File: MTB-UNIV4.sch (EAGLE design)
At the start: 116 parts, among them IC1 MEGA128-A, IC2 SN75176BP, IC3 MC7805CDTG, IC4 ULN2803A, IC5 ULN2803A, Q1 14.745 MHz, X1A MVE252-5-V, X1B MVE252-5-V, X2A MVE252-5-V, X2B MVE252-5-V, X3 1751316, X4 1751316, X5 1751316, X6 1751316

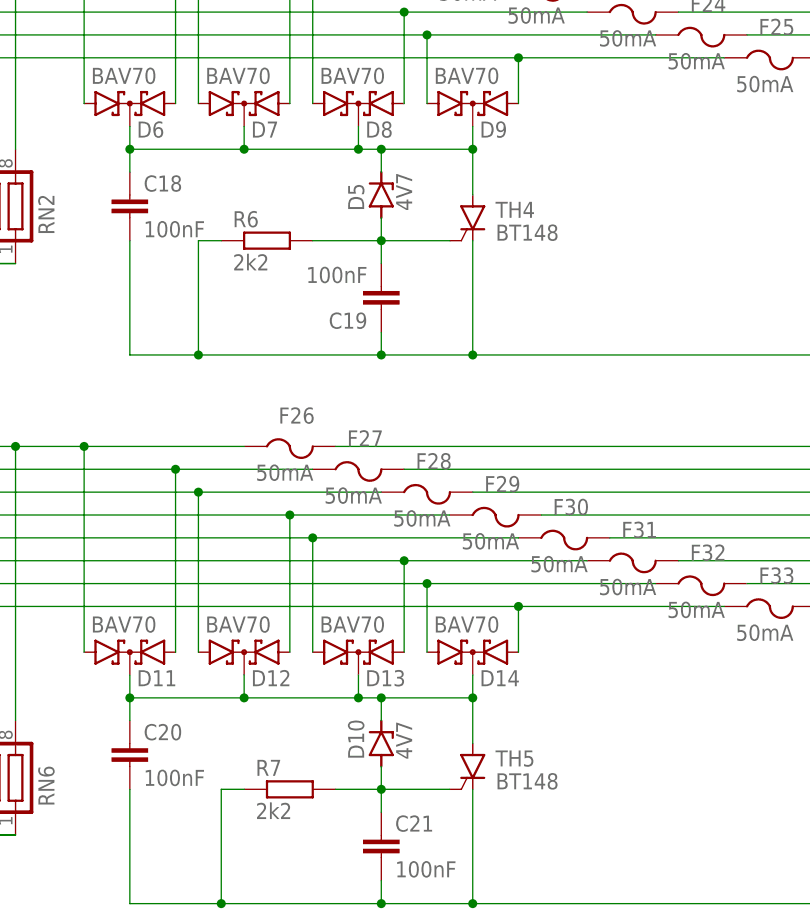
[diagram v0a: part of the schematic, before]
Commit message: Revert zener diodes on inputs to 5V1.
5V1 diodes open tyrristor at ~4V8.
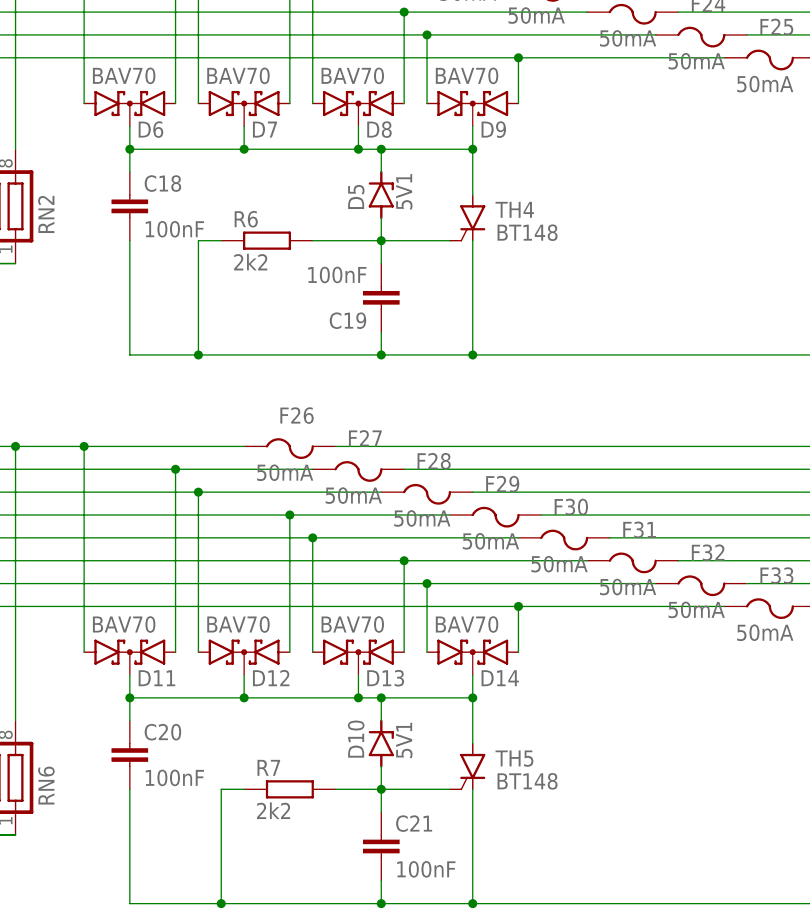
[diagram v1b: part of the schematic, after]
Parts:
- D10, D5: value 4V7 -> 5V1; LCSC_PART C384560 -> C294621
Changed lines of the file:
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@@
 <attribute name="LCSC_PART" value="C261946"/>
 </part>
-<part name="D5" library="diode" library_urn="urn:adsk.eagle:library:210" deviceset="ZENER-DIODE" device="SOT23" package3d_urn="urn:adsk.eagle:package:43389/2" value="4V7">
-<attribute name="LCSC_PART" value="C384560"/>
+<part name="D5" library="diode" library_urn="urn:adsk.eagle:library:210" deviceset="ZENER-DIODE" device="SOT23" package3d_urn="urn:adsk.eagle:package:43389/2" value="5V1">
+<attribute name="LCSC_PART" value="C294621"/>
 </part>
 <part name="R6" library="rcl" deviceset="R-EU_" device="R0805" value="2k2">
@@
 <attribute name="LCSC_PART" value="C261946"/>
 </part>
-<part name="D10" library="diode" library_urn="urn:adsk.eagle:library:210" deviceset="ZENER-DIODE" device="SOT23" package3d_urn="urn:adsk.eagle:package:43389/2" value="4V7">
-<attribute name="LCSC_PART" value="C384560"/>
+<part name="D10" library="diode" library_urn="urn:adsk.eagle:library:210" deviceset="ZENER-DIODE" device="SOT23" package3d_urn="urn:adsk.eagle:package:43389/2" value="5V1">
+<attribute name="LCSC_PART" value="C294621"/>
 </part>
 <part name="R7" library="rcl" deviceset="R-EU_" device="R0805" value="2k2">

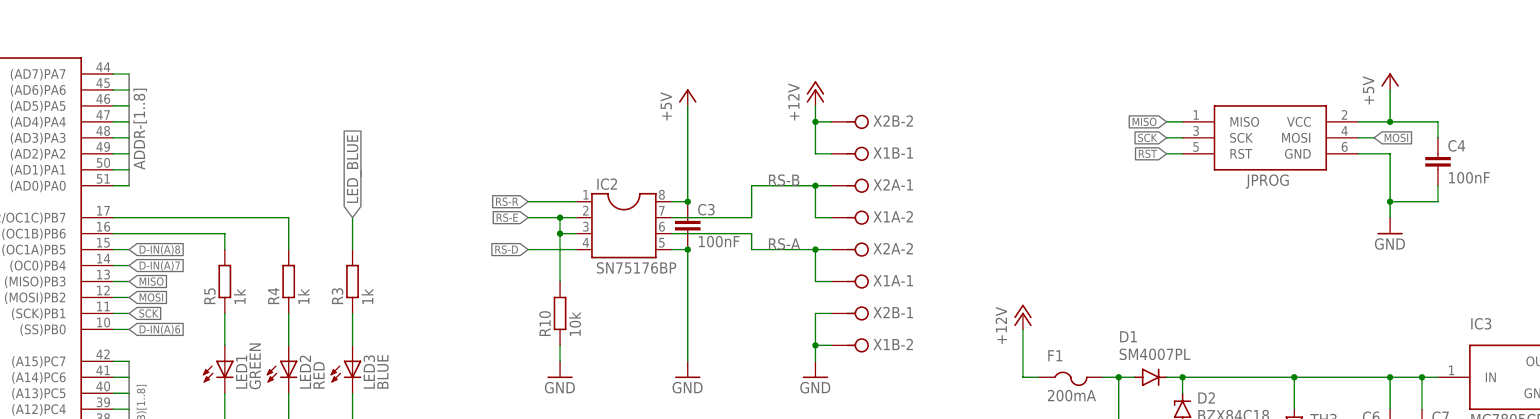
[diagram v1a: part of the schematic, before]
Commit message: Add right MCU pins to programming connector.
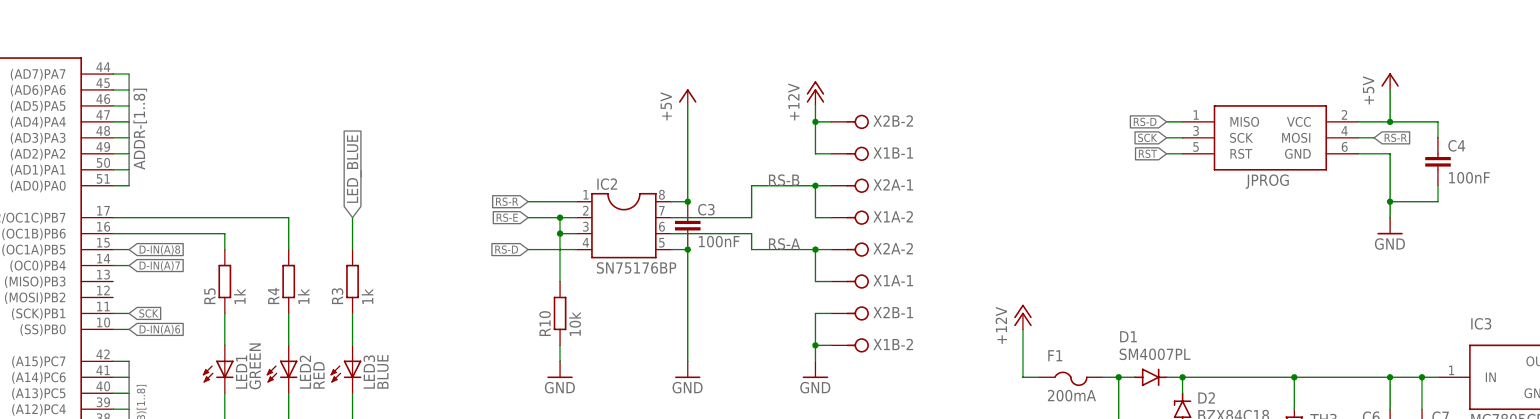
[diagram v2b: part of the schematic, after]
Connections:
- removed net MISO: IC1.(MISO)PB3, JPROG.MISO
- removed net MOSI: IC1.(MOSI)PB2, JPROG.MOSI
- net RS-D: now also JPROG.MISO
- net RS-R: now also JPROG.MOSI
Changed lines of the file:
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@@
-</segment>
-</net>
-<net name="MISO" class="0">
-<segment>
-<pinref part="IC1" gate="G$1" pin="(MISO)PB3"/>
-<wire x1="121.92" y1="88.9" x2="124.46" y2="88.9" width="0.1524" layer="91"/>
-<label x="124.46" y="88.9" size="1.27" layer="95" xref="yes"/>
-</segment>
-<segment>
-<wire x1="292.1" y1="114.3" x2="289.56" y2="114.3" width="0.1524" layer="91"/>
-<label x="289.56" y="114.3" size="1.27" layer="95" rot="R180" xref="yes"/>
-<pinref part="JPROG" gate="G$1" pin="MISO"/>
-</segment>
-</net>
-<net name="MOSI" class="0">
-<segment>
-<pinref part="IC1" gate="G$1" pin="(MOSI)PB2"/>
-<wire x1="121.92" y1="86.36" x2="124.46" y2="86.36" width="0.1524" layer="91"/>
-<label x="124.46" y="86.36" size="1.27" layer="95" xref="yes"/>
-</segment>
-<segment>
-<wire x1="320.04" y1="111.76" x2="322.58" y2="111.76" width="0.1524" layer="91"/>
-<label x="322.58" y="111.76" size="1.27" layer="95" xref="yes"/>
-<pinref part="JPROG" gate="G$1" pin="MOSI"/>
 </segment>
 </net>
@@
 <label x="124.46" y="12.7" size="1.27" layer="95" xref="yes"/>
 </segment>
+<segment>
+<wire x1="320.04" y1="111.76" x2="322.58" y2="111.76" width="0.1524" layer="91"/>
+<label x="322.58" y="111.76" size="1.27" layer="95" xref="yes"/>
+<pinref part="JPROG" gate="G$1" pin="MOSI"/>
+</segment>
 </net>
 <net name="RS-E" class="0">
@@
 <label x="124.46" y="15.24" size="1.27" layer="95" xref="yes"/>
 </segment>
-</net>
+<segment>
+<wire x1="292.1" y1="114.3" x2="289.56" y2="114.3" width="0.1524" layer="91"/>
+<label x="289.56" y="114.3" size="1.27" layer="95" rot="R180" xref="yes"/>
+<pinref part="JPROG" gate="G$1" pin="MISO"/>
+</segment>
+</net>

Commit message: Fix LCSC part of resonator's capacitors.
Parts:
- C1, C2: LCSC_PART C17513 -> C1804
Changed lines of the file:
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@@
 <part name="P+3" library="supply1" library_urn="urn:adsk.eagle:library:371" deviceset="+5V" device=""/>
 <part name="C1" library="rcl" deviceset="C-EU" device="C0805" value="22pF">
-<attribute name="LCSC_PART" value="C17513"/>
+<attribute name="LCSC_PART" value="C1804"/>
 </part>
 <part name="C2" library="rcl" deviceset="C-EU" device="C0805" value="22pF">
-<attribute name="LCSC_PART" value="C17513"/>
+<attribute name="LCSC_PART" value="C1804"/>
 </part>
 <part name="IC2" library="ic-package" library_urn="urn:adsk.eagle:library:239" deviceset="DIL8" device="" package3d_urn="urn:adsk.eagle:package:29519/2" value="SN75176BP"/>

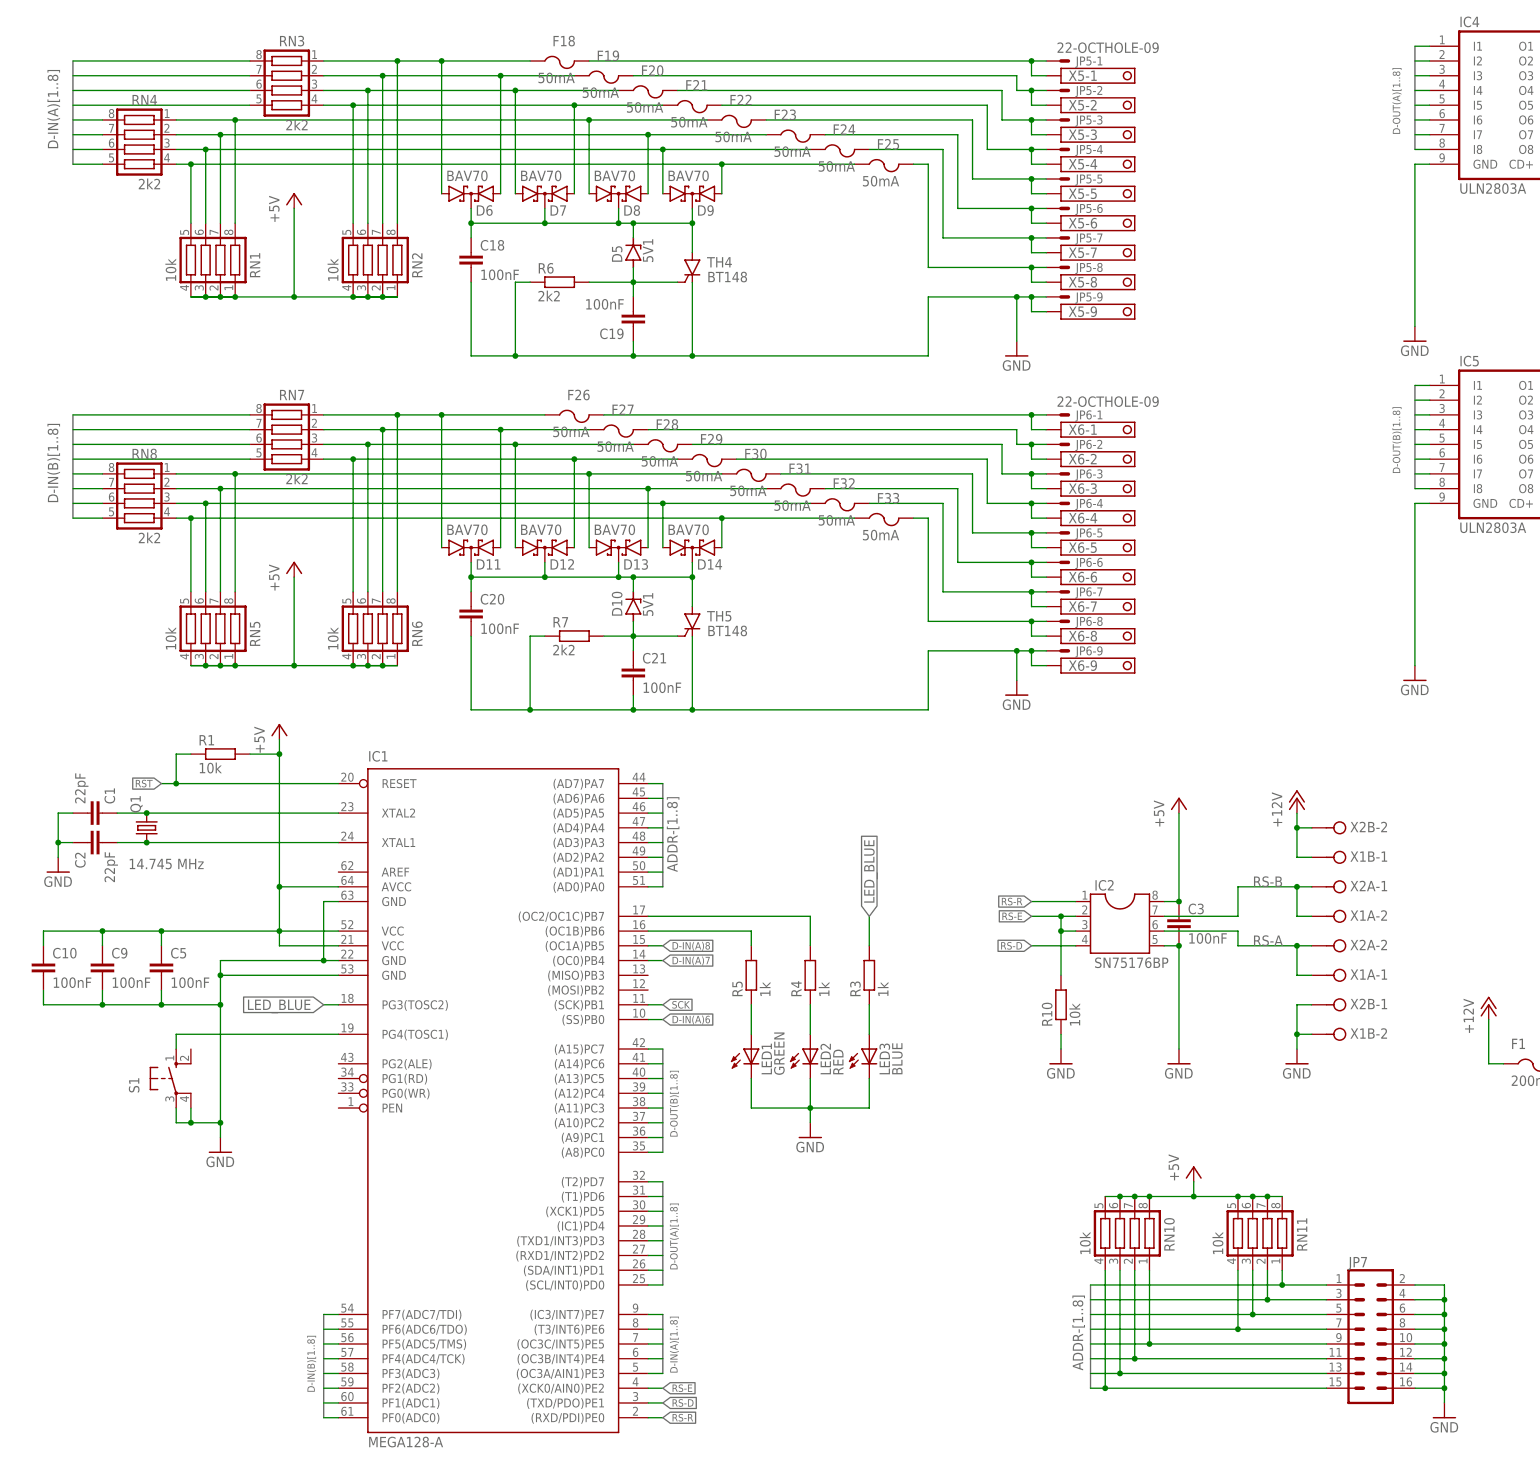
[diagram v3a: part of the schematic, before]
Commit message: Name almost all wires properly.
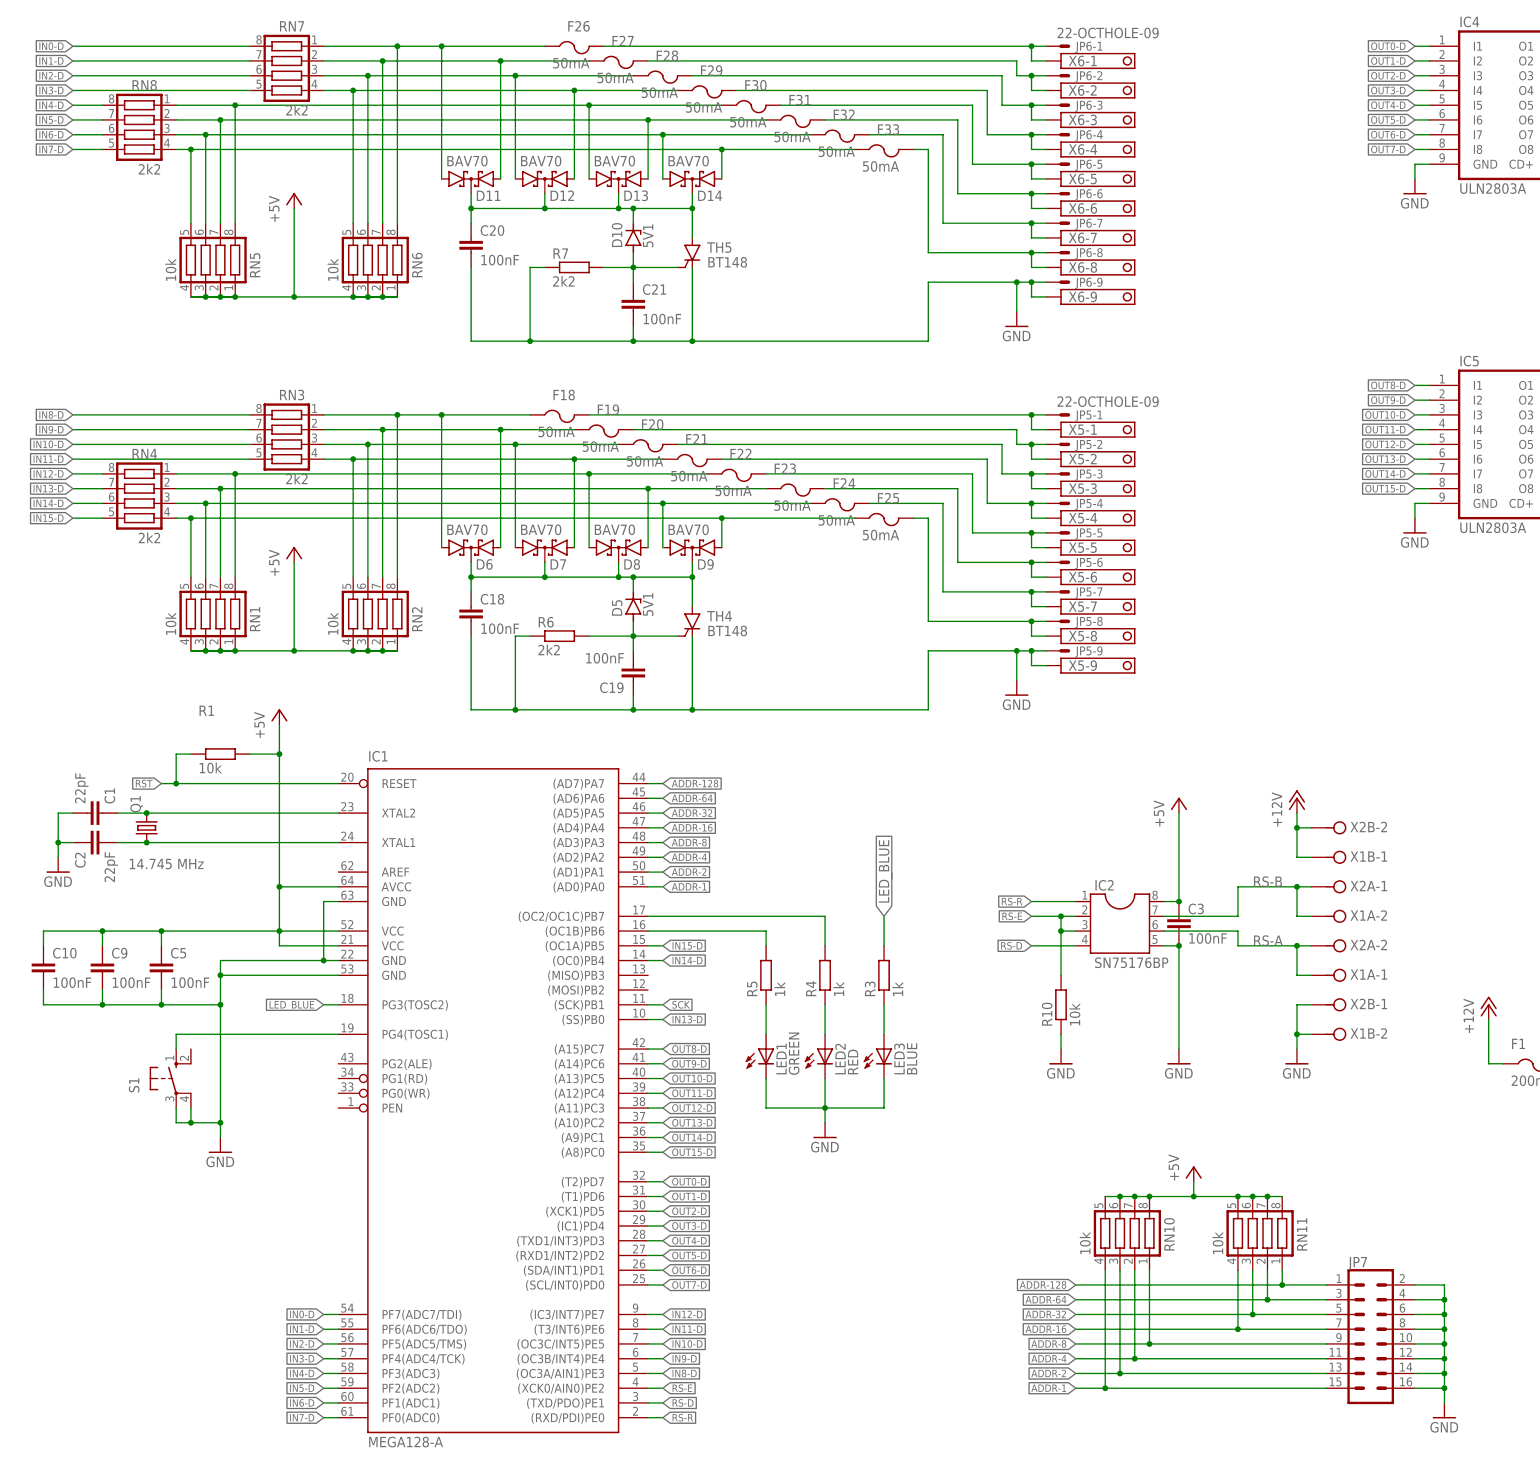
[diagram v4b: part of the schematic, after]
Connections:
- net ADDR-3 renamed ADDR-32
- net D-IN(A)1 renamed IN8-D
- net D-IN(A)2 renamed IN9-D
- net D-IN(A)3 renamed IN10-D
- net D-IN(A)4 renamed IN11-D
- net D-IN(A)5 renamed IN12-D
- net D-IN(A)6 renamed IN13-D
- net D-IN(A)7 renamed IN14-D
- net D-IN(A)8 renamed IN15-D
- net D-IN(B)1 renamed IN0-D
- net D-IN(B)2 renamed IN1-D
- net D-IN(B)3 renamed IN2-D
- net D-IN(B)4 renamed IN3-D
- net D-IN(B)5 renamed IN4-D
- net D-IN(B)6 renamed IN5-D
- net D-IN(B)7 renamed IN6-D
- net D-IN(B)8 renamed IN7-D
- net D-OUT(A)1 renamed OUT0-D
- net D-OUT(A)2 renamed OUT1-D
- net D-OUT(A)3 renamed OUT2-D
- net D-OUT(A)4 renamed OUT3-D
- net D-OUT(A)5 renamed OUT4-D
- net D-OUT(A)6 renamed OUT5-D
- net D-OUT(A)7 renamed OUT6-D
- net D-OUT(A)8 renamed OUT7-D
- net D-OUT(B)1 renamed OUT8-D
- net D-OUT(B)2 renamed OUT9-D
- net D-OUT(B)3 renamed OUT10-D
- net D-OUT(B)4 renamed OUT11-D
- net D-OUT(B)5 renamed OUT12-D
- net D-OUT(B)6 renamed OUT13-D
- net D-OUT(B)7 renamed OUT14-D
- net D-OUT(B)8 renamed OUT15-D
- net N$1 renamed XTAL1
- net N$10 renamed OUT7-R
- net N$12 renamed OUT8-R
- net N$13 renamed +12V-IN
- net N$15 renamed OUT9-R
- net N$16 renamed OUT10-R
- net N$17 renamed OUT11-R
- net N$18 renamed OUT12-R
- net N$19 renamed OUT13-R
- net N$2 renamed OUT0-R
- net N$20 renamed OUT14-R
- net N$21 renamed IN0-R
- net N$22 renamed IN1-R
- net N$23 renamed IN2-R
- net N$24 renamed IN3-R
- net N$25 renamed IN4-R
- net N$26 renamed IN5-R
- net N$27 renamed IN6-R
- net N$28 renamed IN7-R
- net N$29 renamed IN8-R
- net N$3 renamed XTAL2
- net N$30 renamed IN9-R
- net N$31 renamed IN10-R
- net N$32 renamed IN11-R
- net N$33 renamed IN12-R
- net N$34 renamed IN13-R
- net N$35 renamed IN14-R
- net N$36 renamed IN15-R
- net N$38 renamed OUT7-U
- net N$39 renamed OUT6-U
- net N$4 renamed OUT1-R
- net N$40 renamed OUT5-U
- net N$41 renamed OUT4-U
- net N$42 renamed OUT3-U
- net N$43 renamed OUT2-U
- net N$44 renamed OUT-1U
- net N$45 renamed OUT0-U
- net N$47 renamed OUT15-R
- net N$48 renamed OUT15-U
- net N$49 renamed OUT14-U
- net N$5 renamed OUT2-R
- net N$50 renamed OUT13-U
- net N$51 renamed OUT12-U
- net N$52 renamed OUT11-U
- net N$53 renamed OUT10-U
- net N$54 renamed OUT9-U
- net N$55 renamed OUT8-U
- net N$58 renamed +12V_MIN
- net N$6 renamed OUT3-R
- net N$62 renamed IN0-U
- net N$66 renamed IN12-U
- net N$67 renamed IN13-U
- net N$68 renamed IN14-U
- net N$69 renamed IN15-U
- net N$7 renamed OUT4-R
- net N$73 renamed IN1-U
- net N$74 renamed IN2-U
- net N$75 renamed IN3-U
- net N$76 renamed IN4-U
- net N$77 renamed IN5-U
- net N$78 renamed IN6-U
- net N$79 renamed IN7-U
- net N$8 renamed OUT5-R
- net N$86 renamed BTN
- net N$87 renamed IN8-U
- net N$88 renamed IN9-U
- net N$89 renamed IN10-U
- net N$9 renamed OUT6-R
- net N$90 renamed IN11-U
- removed net ADDR-5: IC1.(AD3)PA3, JP7.9, RN10.1
- removed net ADDR-6: IC1.(AD2)PA2, JP7.11, RN10.2
- removed net ADDR-7: IC1.(AD1)PA1, JP7.13, RN10.3
- new net ADDR-128: IC1.(AD7)PA7, JP7.1, RN11.1
- new net ADDR-16: IC1.(AD4)PA4, JP7.7, RN11.4
- new net ADDR-64: IC1.(AD6)PA6, JP7.3, RN11.2
- net ADDR-1: now also IC1.(AD0)PA0, JP7.15, RN10.4; no longer IC1.(AD7)PA7, JP7.1, RN11.1
- net ADDR-2: now also IC1.(AD1)PA1, JP7.13, RN10.3; no longer IC1.(AD6)PA6, JP7.3, RN11.2
- net ADDR-4: now also IC1.(AD2)PA2, JP7.11, RN10.2; no longer IC1.(AD4)PA4, JP7.7, RN11.4
- net ADDR-8: now also IC1.(AD3)PA3, JP7.9, RN10.1; no longer IC1.(AD0)PA0, JP7.15, RN10.4
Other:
- moved on the sheet: C18, C19, C20, C21, D10, D11, D12, D13, D14, D5, D6, D7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
